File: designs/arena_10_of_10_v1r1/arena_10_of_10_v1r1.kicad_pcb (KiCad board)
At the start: 6 copper layers, 248.9 x 228.6 mm, 519 parts, among them J1 Cetus RJ45 Magjack, J10 Conn_01x05, J11 Conn_01x05, J12 Conn_01x05, J13 Conn_01x05, J14 Conn_01x05, J15 Conn_01x05, J16 Conn_01x05, J17 Conn_01x05, J18 Conn_01x05, J19 Conn_01x05, J2 Conn_01x02, J20 Conn_01x05, J21 Conn_01x05, J22 Conn_01x05, J23 Conn_01x05, J24 Conn_01x05, J25 Barrel_Jack, J26 Barrel_Jack, J27 Conn_Coaxial, J28 Conn_Coaxial, J29 Conn_Coaxial, J3 Conn_Coaxial, J4 Conn_Coaxial, J5 Conn_01x05, J6 Conn_01x05, J7 Conn_01x05, J8 Conn_01x05, J9 Conn_01x05, P1 NA, P10 NA, P2 NA, P3 NA, P4 NA, P5 NA, P6 NA, P7 NA, P8 NA, P9 NA, SW1 SW_SPDT, U1 Teensy4.1, U10 74LVC2G17, U100 74LVC1G125, U101 74LVC2G17, U102 SN74HCS08, U103 SN74HCS08, U104 74LVC1G125, U105 74LVC2G17, U106 SN74HCS08, U107 SN74HCS08, U108 74LVC1G125, U109 74LVC2G17, U11 74LVC2G17, U112 74LVC1G125, U113 74LVC2G17, U116 74LVC1G125, U117 74LVC2G17, U12 74LVC2G17, U120 74LVC1G125, U121 74LVC2G17, U124 74LVC1G125, U125 74LVC2G17, U13 74LVC2G17, U14 74LVC2G17, U15 74LVC2G17, U16 74LVC2G17, U17 74LVC2G17, U18 74LVC2G17, U19 74LVC2G17, U2 SN74LV1T34DBV, U20 74LVC2G17, U21 74LVC2G17, U22 74LVC2G17, U23 74LVC2G17, U24 74LVC2G17, U25 74LVC2G17, U26 74LVC2G17, U27 74LVC2G17, U28 74LVC2G17, U29 74LVC2G17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

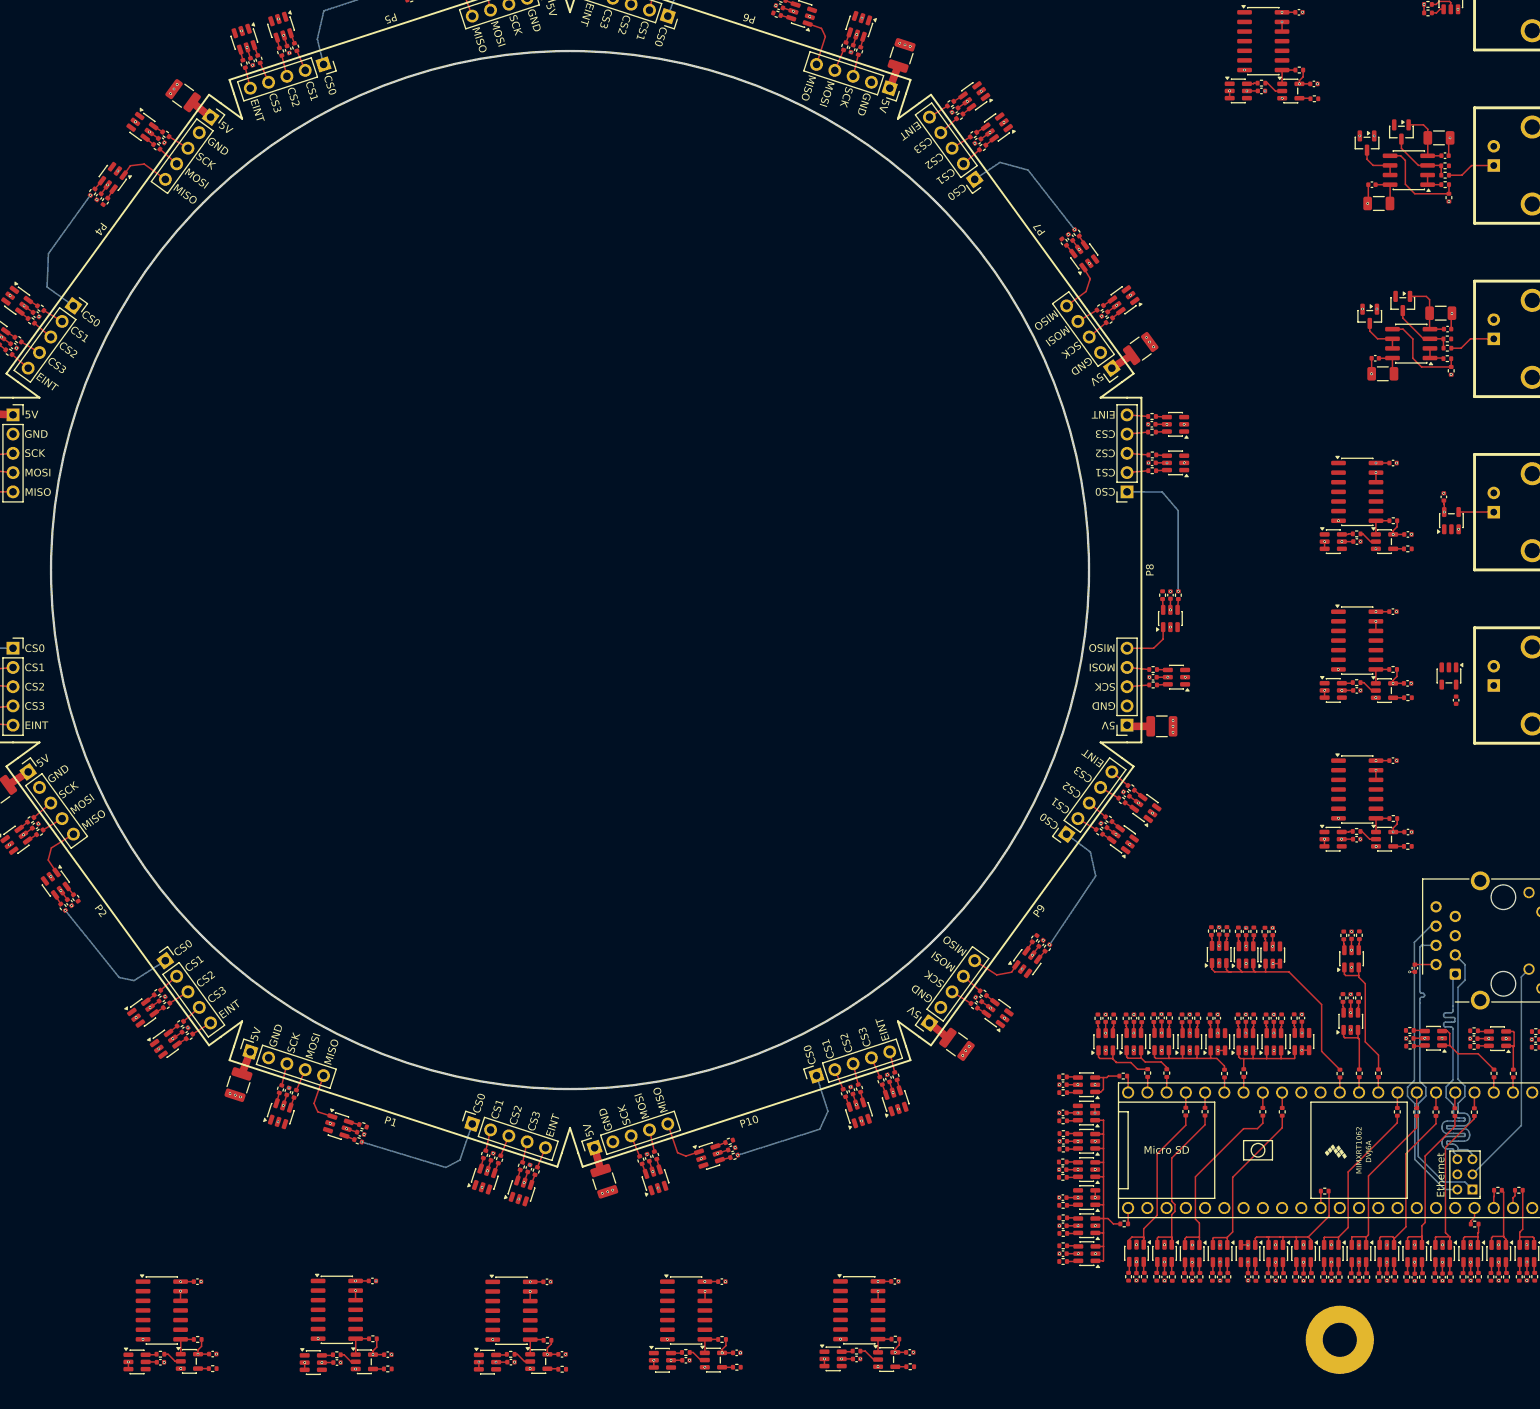
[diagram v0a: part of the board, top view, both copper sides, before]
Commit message: Minor mods to pcb layout to help with auto-routing.
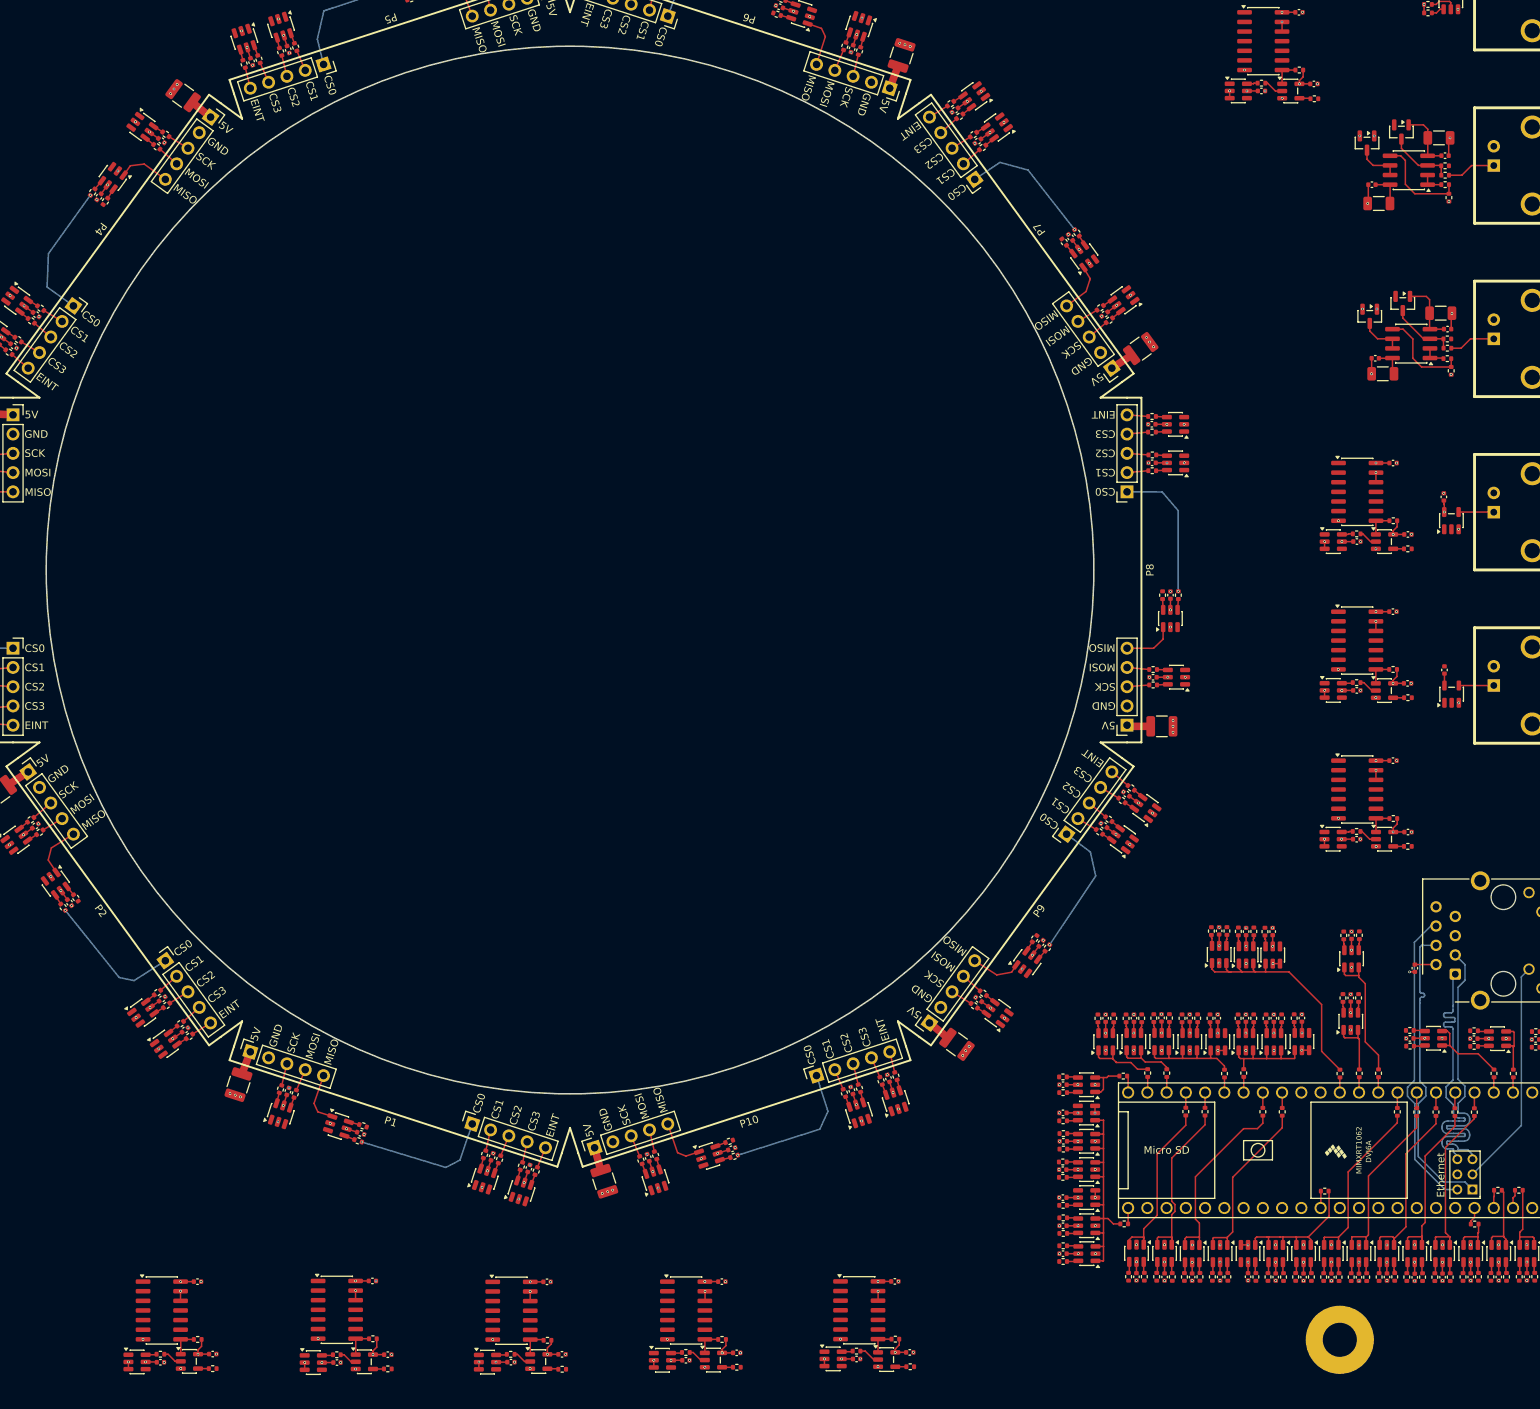
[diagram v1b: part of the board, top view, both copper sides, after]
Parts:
- moved C2 4.28 mm to (293.2, 191.0), turned to 90 degrees
- moved U2 2.42 mm to (294.2, 194.2), turned to 90 degrees
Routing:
- net /Teensy/D36_5V: track 0.00 -> 4.61 mm
- net +5V: track 36.9 -> 38.5 mm
- net GND: vias 279 -> 280
- net +3.3V: vias 110 -> 111
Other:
- outline, holes or cut-outs redrawn
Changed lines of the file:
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@@
 	(footprint "Capacitor_SMD:C_0402_1005Metric"
 		(layer "F.Cu")
-		(at 294.75 194.98 -90)
+		(at 293.21 190.99 90)
 		(descr "Capacitor SMD 0402 (1005 Metric), square (rectangular) end terminal, IPC-7351 nominal, (Body size source: IPC-SM-782 page 76, https://www.pcb-3d.com/wordpress/wp-content/uploads/ipc-sm-782a_amendment_1_and_2.pdf), generated with kicad-footprint-generator")
 		(tags "capacitor")
@@
 		)
 		(property "LCSC Part #" "C1525"
-			(at 0 0 270)
+			(at 0 0 90)
 			(unlocked yes)
 			(layer "F.Fab")
@@
 		(attr smd)
 		(fp_line
-			(start -0.107836 0.36)
-			(end 0.107836 0.36)
+			(start -0.107836 -0.36)
+			(end 0.107836 -0.36)
 			(stroke
 				(width 0.12)
@@
 		)
 		(fp_line
-			(start -0.107836 -0.36)
-			(end 0.107836 -0.36)
+			(start -0.107836 0.36)
+			(end 0.107836 0.36)
 			(stroke
 				(width 0.12)
@@
 		)
 		(fp_line
-			(start -0.91 0.46)
-			(end -0.91 -0.46)
+			(start 0.91 -0.46)
+			(end 0.91 0.46)
 			(stroke
 				(width 0.05)
@@
 		)
 		(fp_line
-			(start 0.91 0.46)
-			(end -0.91 0.46)
+			(start -0.91 -0.46)
+			(end 0.91 -0.46)
 			(stroke
 				(width 0.05)
@@
 		)
 		(fp_line
-			(start -0.91 -0.46)
-			(end 0.91 -0.46)
+			(start 0.91 0.46)
+			(end -0.91 0.46)
 			(stroke
 				(width 0.05)
@@
 		)
 		(fp_line
-			(start 0.91 -0.46)
-			(end 0.91 0.46)
+			(start -0.91 0.46)
+			(end -0.91 -0.46)
 			(stroke
 				(width 0.05)
@@
 		)
 		(fp_line
-			(start -0.5 0.25)
-			(end -0.5 -0.25)
+			(start 0.5 -0.25)
+			(end 0.5 0.25)
 			(stroke
 				(width 0.1)
@@
 		)
 		(fp_line
-			(start 0.5 0.25)
-			(end -0.5 0.25)
+			(start -0.5 -0.25)
+			(end 0.5 -0.25)
 			(stroke
 				(width 0.1)
@@
 		)
 		(fp_line
-			(start -0.5 -0.25)
-			(end 0.5 -0.25)
+			(start 0.5 0.25)
+			(end -0.5 0.25)
 			(stroke
 				(width 0.1)
@@
 		)
 		(fp_line
-			(start 0.5 -0.25)
-			(end 0.5 0.25)
+			(start -0.5 0.25)
+			(end -0.5 -0.25)
 			(stroke
 				(width 0.1)
@@
 		)
 		(pad "1" smd roundrect
-			(at -0.48 0 270)
+			(at -0.48 0 90)
 			(size 0.56 0.62)
 			(layers "F.Cu" "F.Mask" "F.Paste")
@@
 		)
 		(pad "2" smd roundrect
-			(at 0.48 0 270)
+			(at 0.48 0 90)
 			(size 0.56 0.62)
 			(layers "F.Cu" "F.Mask" "F.Paste")
@@
 	(footprint "Package_TO_SOT_SMD:SOT-23-5"
 		(layer "F.Cu")
-		(at 293.8 191.7875 -90)
+		(at 294.16 194.1825 90)
 		(descr "SOT, 5 Pin (JEDEC MO-178 Var AA https://www.jedec.org/document_search?search_api_views_fulltext=MO-178), generated with kicad-footprint-generator ipc_gullwing_generator.py")
 		(tags "SOT TO_SOT_SMD")
@@
 		(attr smd)
 		(fp_line
-			(start -0.91 1.56)
-			(end -0.91 1.51)
+			(start 0.91 -1.56)
+			(end 0.91 -1.51)
 			(stroke
 				(width 0.12)
@@
 		)
 		(fp_line
-			(start 0.91 1.56)
-			(end -0.91 1.56)
+			(start -0.91 -1.56)
+			(end 0.91 -1.56)
 			(stroke
 				(width 0.12)
@@
 		)
 		(fp_line
-			(start 0.91 1.51)
-			(end 0.91 1.56)
+			(start -0.91 -1.51)
+			(end -0.91 -1.56)
 			(stroke
 				(width 0.12)
@@
 		)
 		(fp_line
-			(start -0.91 -1.51)
-			(end -0.91 -1.56)
+			(start 0.91 1.51)
+			(end 0.91 1.56)
 			(stroke
 				(width 0.12)
@@
 		)
 		(fp_line
-			(start -0.91 -1.56)
-			(end 0.91 -1.56)
+			(start 0.91 1.56)
+			(end -0.91 1.56)
 			(stroke
 				(width 0.12)
@@
 		)
 		(fp_line
-			(start 0.91 -1.56)
-			(end 0.91 -1.51)
+			(start -0.91 1.56)
+			(end -0.91 1.51)
 			(stroke
 				(width 0.12)
@@
 		)
 		(fp_line
-			(start -1.05 1.7)
-			(end -1.05 1.5)
+			(start 1.05 -1.7)
+			(end 1.05 -1.5)
 			(stroke
 				(width 0.05)
@@
 		)
 		(fp_line
-			(start 1.05 1.7)
-			(end -1.05 1.7)
+			(start -1.05 -1.7)
+			(end 1.05 -1.7)
 			(stroke
 				(width 0.05)
@@
 		)
 		(fp_line
-			(start -2.05 1.5)
-			(end -2.05 -1.5)
+			(start 2.05 -1.5)
+			(end 2.05 1.5)
 			(stroke
 				(width 0.05)
@@
 		)
 		(fp_line
-			(start -1.05 1.5)
-			(end -2.05 1.5)
+			(start 1.05 -1.5)
+			(end 2.05 -1.5)
 			(stroke
 				(width 0.05)
@@
 		)
 		(fp_line
-			(start 1.05 1.5)
-			(end 1.05 1.7)
+			(start -1.05 -1.5)
+			(end -1.05 -1.7)
 			(stroke
 				(width 0.05)
@@
 		)
 		(fp_line
-			(start 2.05 1.5)
-			(end 1.05 1.5)
+			(start -2.05 -1.5)
+			(end -1.05 -1.5)
 			(stroke
 				(width 0.05)
@@
 		)
 		(fp_line
-			(start -2.05 -1.5)
-			(end -1.05 -1.5)
+			(start 2.05 1.5)
+			(end 1.05 1.5)
 			(stroke
 				(width 0.05)
@@
 		)
 		(fp_line
-			(start -1.05 -1.5)
-			(end -1.05 -1.7)
+			(start 1.05 1.5)
+			(end 1.05 1.7)
 			(stroke
 				(width 0.05)
@@
 		)
 		(fp_line
-			(start 1.05 -1.5)
-			(end 2.05 -1.5)
+			(start -1.05 1.5)
+			(end -2.05 1.5)
 			(stroke
 				(width 0.05)
@@
 		)
 		(fp_line
-			(start 2.05 -1.5)
-			(end 2.05 1.5)
+			(start -2.05 1.5)
+			(end -2.05 -1.5)
 			(stroke
 				(width 0.05)
@@
 		)
 		(fp_line
-			(start -1.05 -1.7)
-			(end 1.05 -1.7)
+			(start 1.05 1.7)
+			(end -1.05 1.7)
 			(stroke
 				(width 0.05)
@@
 		)
 		(fp_line
-			(start 1.05 -1.7)
-			(end 1.05 -1.5)
+			(start -1.05 1.7)
+			(end -1.05 1.5)
 			(stroke
 				(width 0.05)
@@
 		)
 		(pad "1" smd roundrect
-			(at -1.1375 -0.95 270)
+			(at -1.1375 -0.95 90)
 			(size 1.325 0.6)
 			(layers "F.Cu" "F.Mask" "F.Paste")
@@
 		)
 		(pad "2" smd roundrect
-			(at -1.1375 0 270)
+			(at -1.1375 0 90)
 			(size 1.325 0.6)
 			(layers "F.Cu" "F.Mask" "F.Paste")
@@
 		)
 		(pad "3" smd roundrect
-			(at -1.1375 0.95 270)
+			(at -1.1375 0.95 90)
 			(size 1.325 0.6)
 			(layers "F.Cu" "F.Mask" "F.Paste")
@@
 		)
 		(pad "4" smd roundrect
-			(at 1.1375 0.95 270)
+			(at 1.1375 0.95 90)
 			(size 1.325 0.6)
 			(layers "F.Cu" "F.Mask" "F.Paste")
@@
 		)
 		(pad "5" smd roundrect
-			(at 1.1375 -0.95 270)
+			(at 1.1375 -0.95 90)
 			(size 1.325 0.6)
 			(layers "F.Cu" "F.Mask" "F.Paste")
@@
 		(layer "Dwgs.User")
 	)
-	(gr_line
-		(start 292.1 63.5)
-		(end 63.5 63.5)
+	(gr_circle
+		(center 177.8 177.8)
+		(end 246.3 177.8)
 		(stroke
 			(width 0.3)
 			(type solid)
 		)
+		(fill no)
 		(layer "Dwgs.User")
 	)
-	(gr_circle
-		(center 177.8 177.8)
-		(end 246.935 177.8)
+	(gr_line
+		(start 292.1 63.5)
+		(end 63.5 63.5)
 		(stroke
-			(width 0.2)
+			(width 0.3)
 			(type solid)
 		)
-		(fill no)
 		(layer "Dwgs.User")
 	)
@@
 	(gr_circle
 		(center 177.8 177.8)
-		(end 246.3 177.8)
+		(end 246.935 177.8)
 		(stroke
-			(width 0.3)
+			(width 0.2)
 			(type solid)
 		)
@@
 	)
 	(segment
+		(start 295.11 195.32)
+		(end 295.1 195.33)
+		(width 0.2)
+		(layer "F.Cu")
+		(net 2)
+	)
+	(segment
 		(start 126.39 274.2475)
 		(end 126.3975 274.255)
@@
 	)
 	(via
+		(at 295.1 195.33)
+		(size 0.35)
+		(drill 0.2)
+		(layers "F.Cu" "B.Cu")
+		(net 2)
+	)
+	(via
 		(at 267.29 271.56)
 		(size 0.35)
@@
 	)
 	(segment
+		(start 293.21 193.045)
+		(end 293.21 191.47)
+		(width 0.2)
+		(layer "F.Cu")
+		(net 3)
+	)
+	(segment
 		(start 134.497475 244.311383)
 		(end 135.604267 241.390439)
@@
 	)
 	(via
+		(at 121.79 282.32)
+		(size 0.35)
+		(drill 0.2)
+		(layers "F.Cu" "B.Cu")
+		(net 4)
+	)
+	(via
 		(at 286.44 212.37)
 		(size 0.35)
@@
 	)
 	(segment
+		(start 299.715 193.045)
+		(end 299.72 193.04)
+		(width 0.2)
+		(layer "F.Cu")
+		(net 22)
+	)
+	(segment
+		(start 295.11 193.045)
+		(end 299.715 193.045)
+		(width 0.2)
+		(layer "F.Cu")
+		(net 22)
+	)
+	(segment
